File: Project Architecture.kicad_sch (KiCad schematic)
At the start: 0 parts

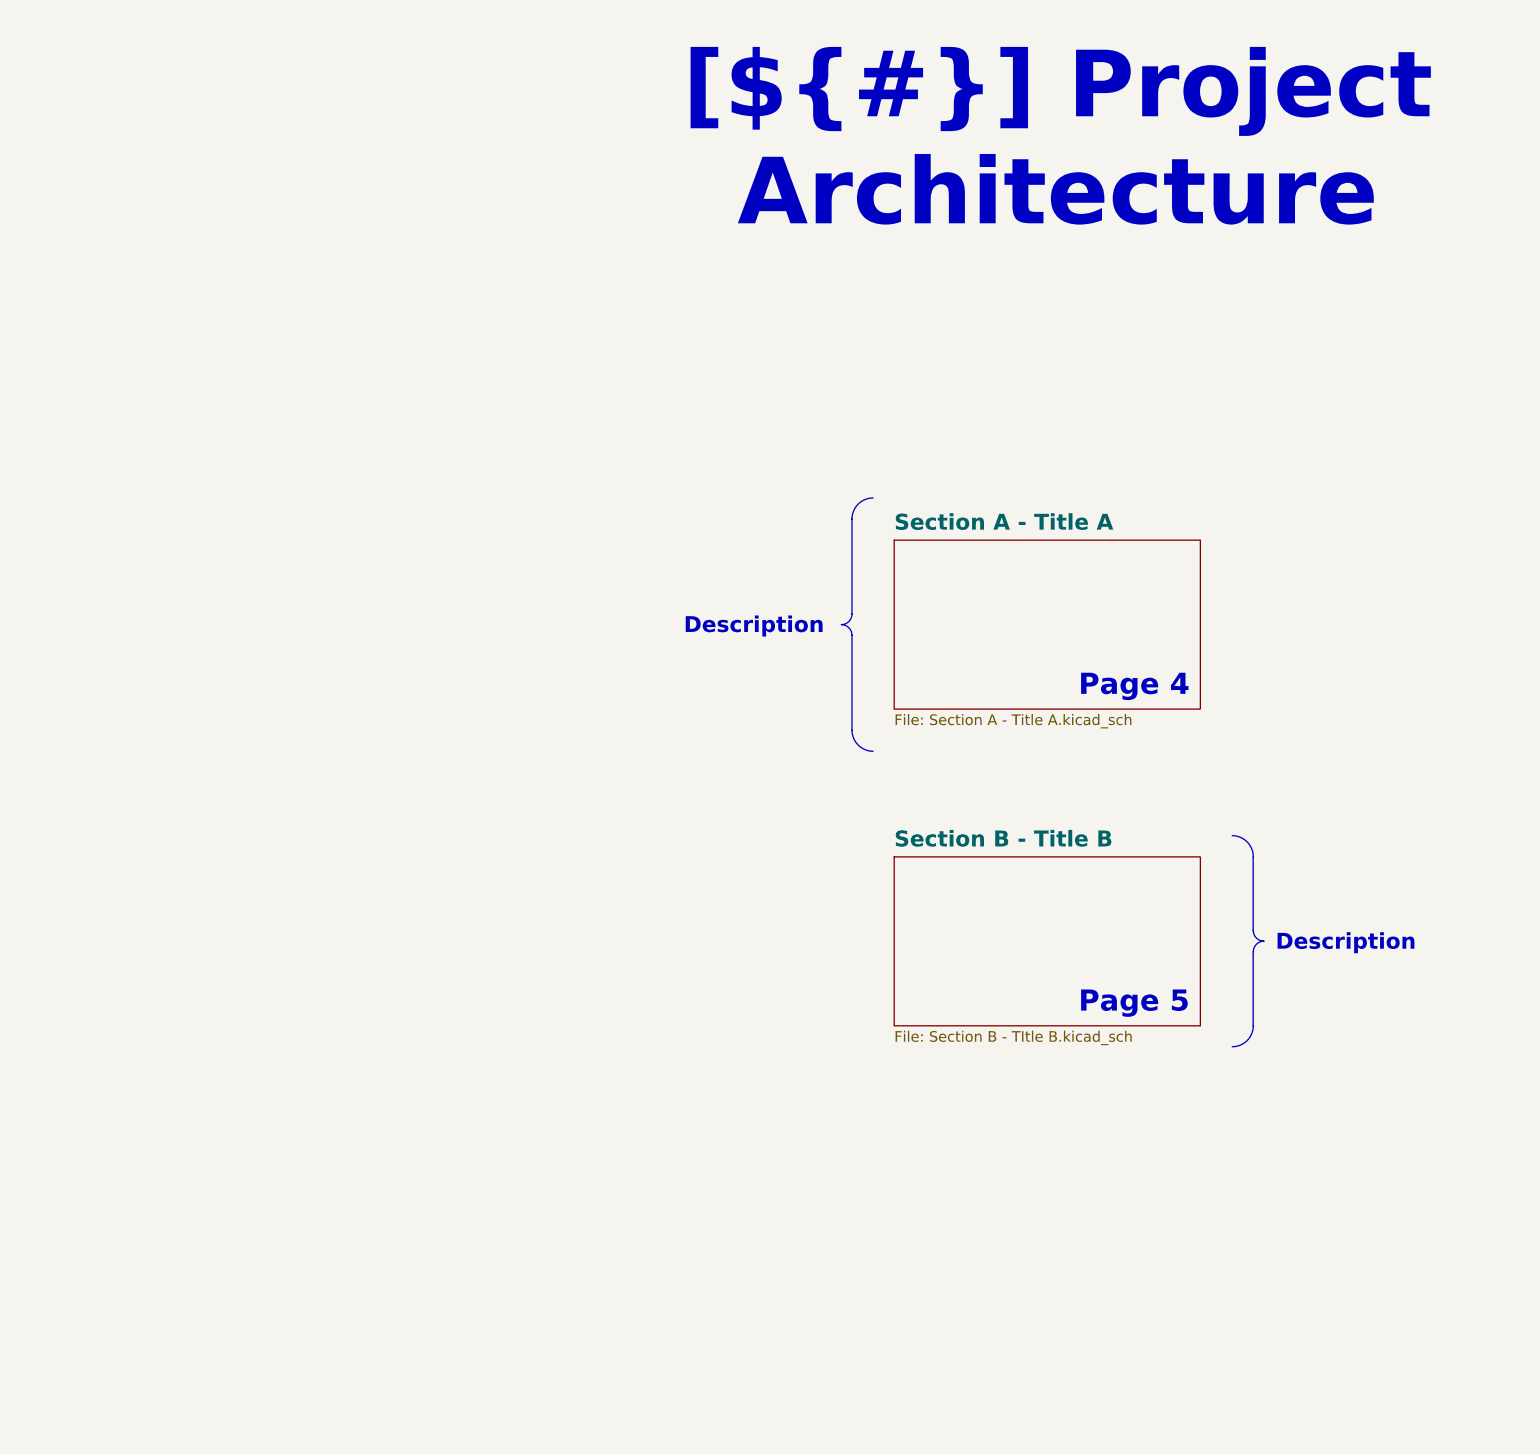
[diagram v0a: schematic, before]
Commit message: add mcu
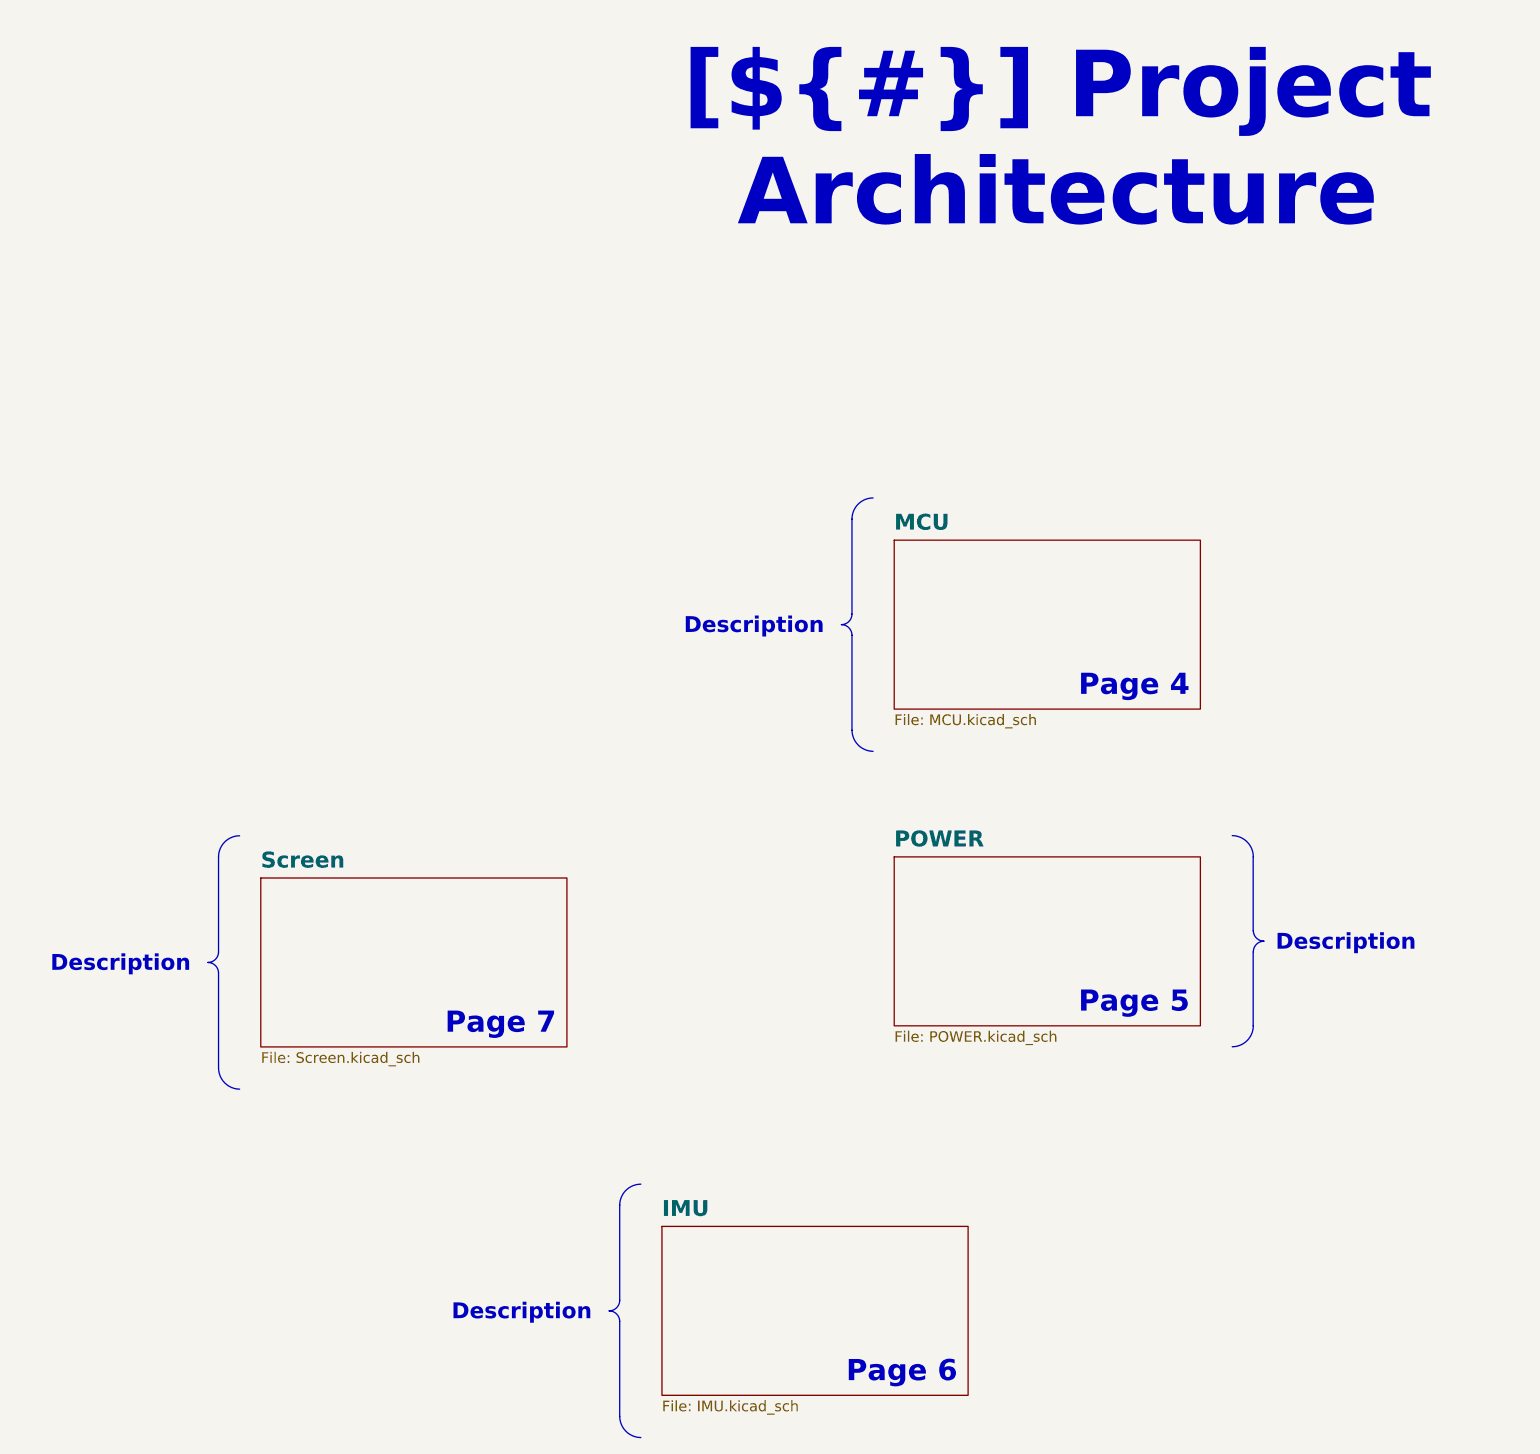
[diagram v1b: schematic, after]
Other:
- sheet Section A - Title A renamed MCU
- sheet Section B - Title B renamed POWER
- added sheet IMU (IMU.kicad_sch)
- added sheet Screen (Screen.kicad_sch)
- sheet MCU: file Section A - Title A.kicad_sch -> MCU.kicad_sch
- sheet POWER: file Section B - TItle B.kicad_sch -> POWER.kicad_sch
- note added: "Page 6"
- note added: "Page 7"
